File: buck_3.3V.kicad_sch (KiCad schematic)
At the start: 16 parts, among them J1101 3.3V Header, U1101 TPS566238PRQFR

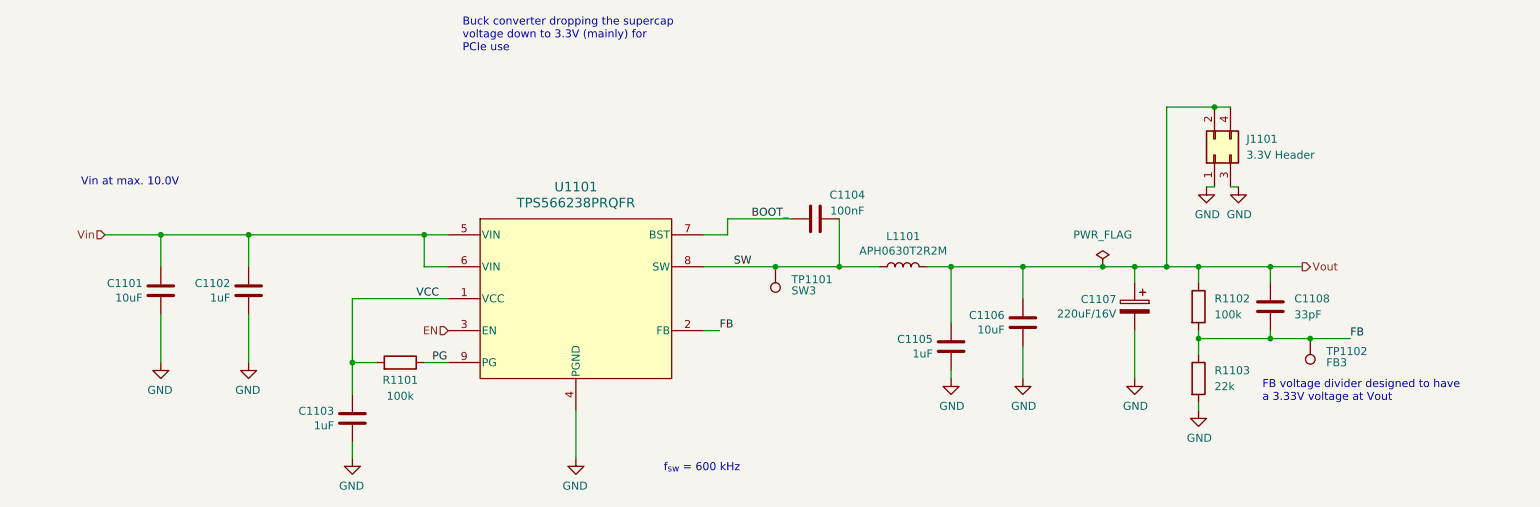
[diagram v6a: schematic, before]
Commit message: Finish transitioning to RP2040
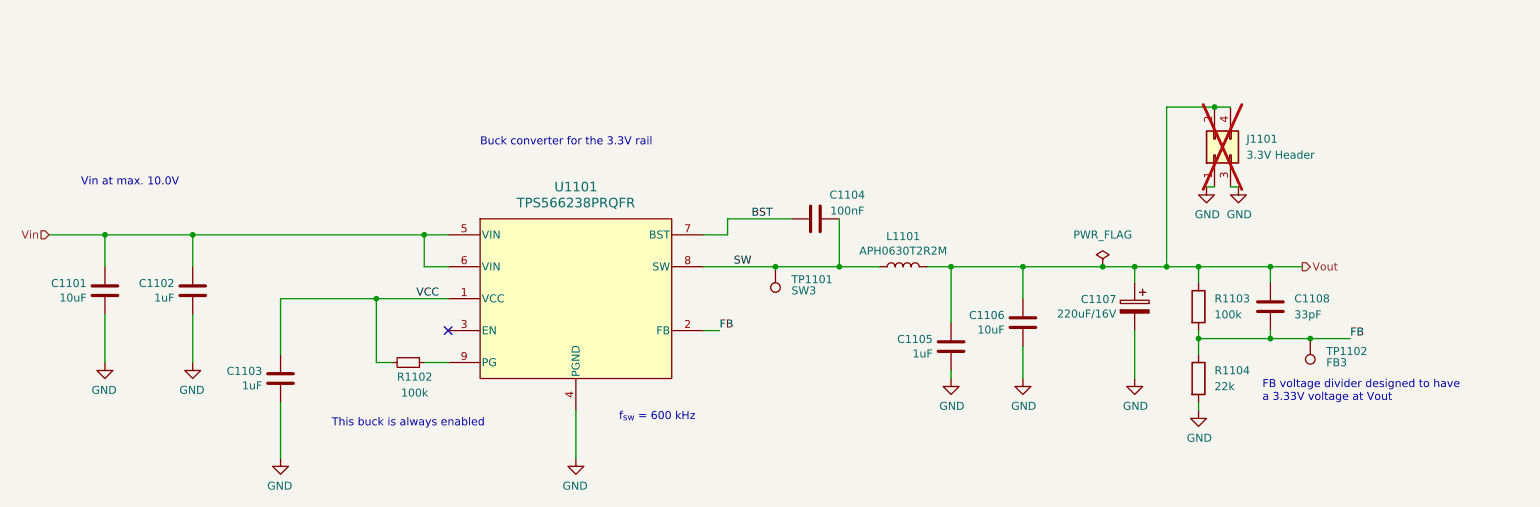
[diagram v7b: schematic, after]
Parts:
- removed R1101: 100k, Resistor_SMD:R_0402_1005Metric, symbol Device:R
- added R1102: 100k, Resistor_SMD:R_0402_1005Metric, symbol Device:R_Small
- J1101: LCSC (none) -> C7501273; now not fitted; now in the parts list
- renumbered R1102 to R1103, R1103 to R1104
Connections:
- net VCC: now also R1102.2
- net BOOT_ renamed BST
- net EN: no longer names the net of U1101.3 (EN)
- net PG: no longer names the net of U1101.9 (PG)
- net PG: now also R1102.1
- no-connect marks 0 -> 1
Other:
- note added: "Buck converter for the 3.3V rail"
- note added: "This buck is always enabled"
- note removed: "Buck converter dropping the supercap voltage down to 3.3V (mainly) for PCIe use"
- moved on the sheet: C1101, C1102, C1103
